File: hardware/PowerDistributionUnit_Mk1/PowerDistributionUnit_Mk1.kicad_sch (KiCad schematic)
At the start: 29 parts, among them J1 XT-30, J2 Molex_NanoFit_2x8, J3 Molex_NanoFit_1x4, J4 Molex_NanoFit_1x2, J5 Molex_NanoFit_1x2, J8 Molex_NanoFit_1x2, J9 Molex_NanoFit_1x2

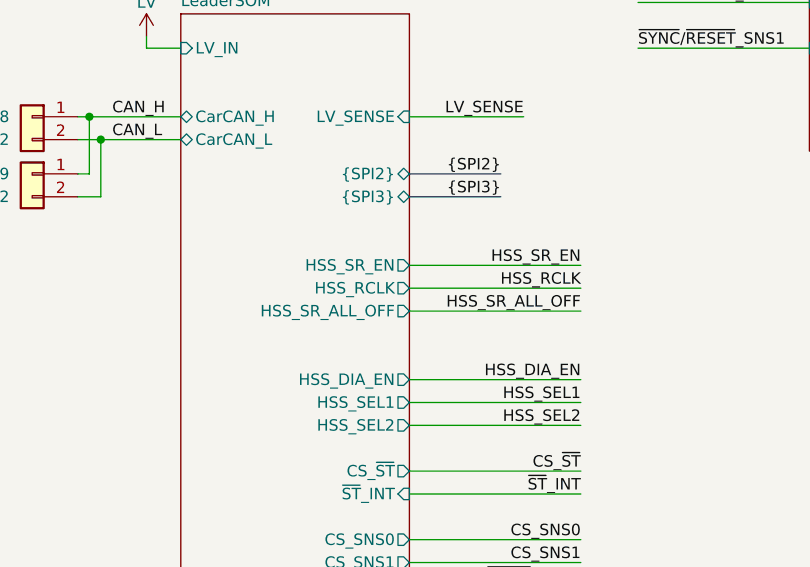
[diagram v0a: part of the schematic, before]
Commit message: routed a couple of logic analyzer connectors, fixed HSS SR out clk label, adjusted logic analyzer pinout
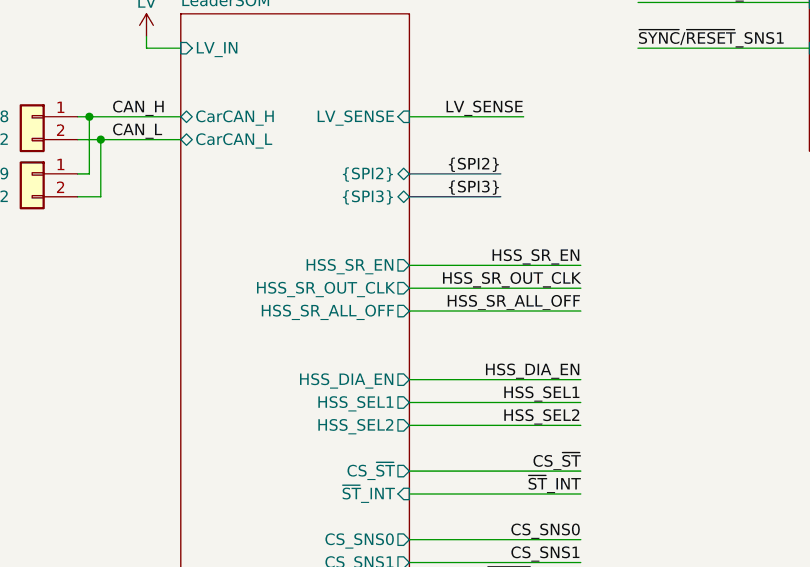
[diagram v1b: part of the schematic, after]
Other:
- sheet LeaderSOM ports: added HSS_SR_OUT_CLK; removed HSS_RCLK
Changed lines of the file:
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@@
 		)
 	)
-	(label "HSS_RCLK"
+	(label "HSS_SR_OUT_CLK"
 		(at 104.14 115.57 180)
 		(effects
@@
 			)
 		)
-		(pin "HSS_RCLK" output
+		(pin "HSS_SR_OUT_CLK" output
 			(at 85.09 115.57 0)
 			(effects

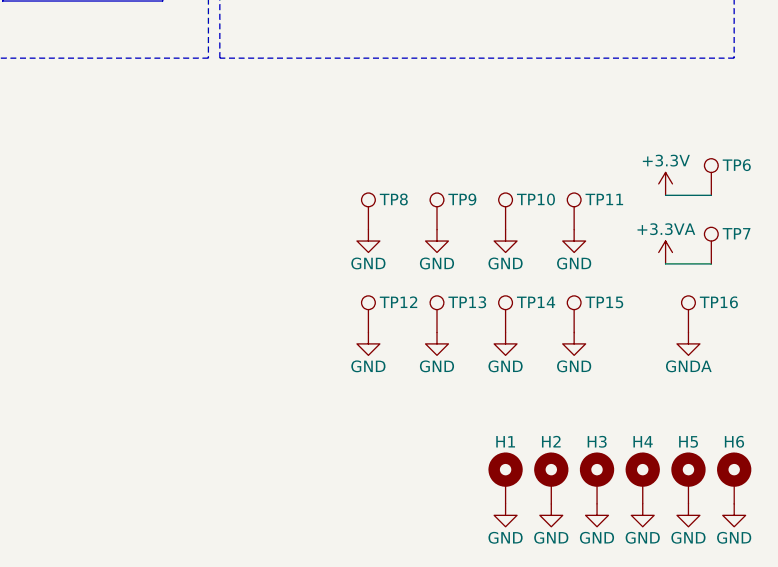
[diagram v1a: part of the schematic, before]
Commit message: gnd test points placement and added some
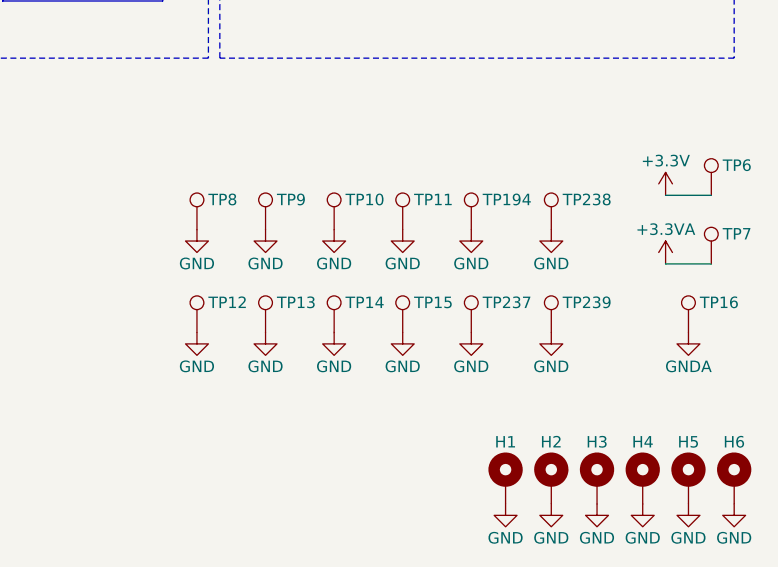
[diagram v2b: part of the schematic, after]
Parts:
- added TP194, TP237, TP238, TP239: TestPoint, Connector_PinHeader_2.54mm:PinHeader_1x01_P2.54mm_Vertical, symbol Connector:TestPoint
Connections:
- net GND: now also TP194.1, TP237.1, TP238.1, TP239.1
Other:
- moved on the sheet: TP10, TP11, TP12, TP13, TP14, TP15, TP8, TP9

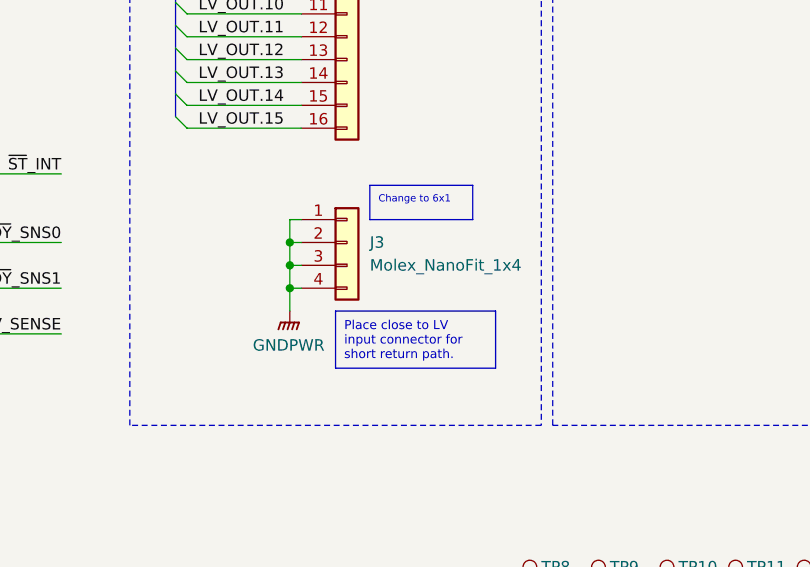
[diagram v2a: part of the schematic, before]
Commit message: change gnd return to 6 pin nanofit
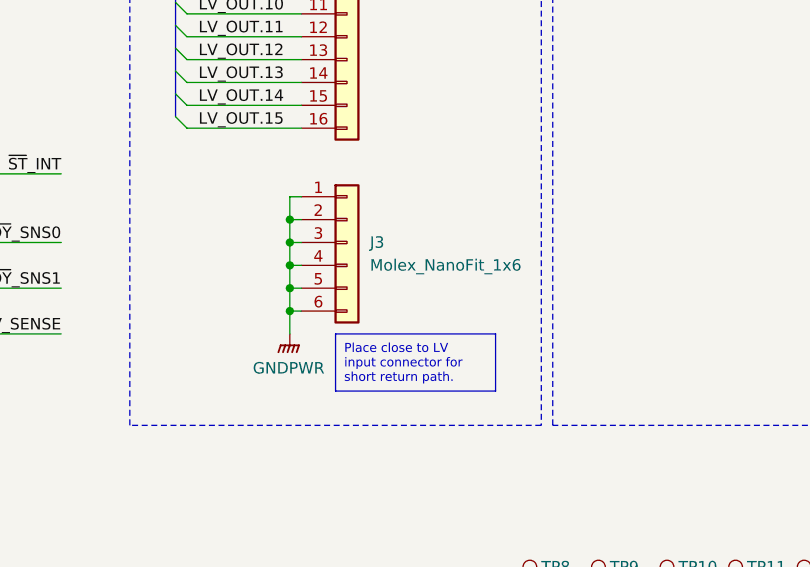
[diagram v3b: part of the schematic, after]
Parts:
- removed J3: Molex_NanoFit_1x4, PowerDistributionUnitLib:CONN_SD-105309-100_04_MOL, symbol PowerDistributionUnitLib:Molex_NanoFit_1x4
- added J3: Molex_NanoFit_1x6, PowerDistributionUnitLib:CONN_SD-105309-100_06_MOL, symbol PowerDistributionUnitLib:Molex_NanoFit_1x6
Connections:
- net GNDPWR: now also J3.1 (Pin_1), J3.2 (Pin_2), J3.3 (Pin_3), J3.4 (Pin_4), J3.5 (Pin_5), J3.6 (Pin_6)
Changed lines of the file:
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@@
 	(text_box "Place close to LV input connector for short return path."
 		(exclude_from_sim no)
-		(at 195.58 93.98 0)
+		(at 195.58 96.52 0)
 		(size 17.78 6.35)
 		(margins 0.9525 0.9525 0.9525 0.9525)
@@
 		)
 	)
-	(text_box "Change to 6x1"
-		(exclude_from_sim no)
-		(at 199.39 80.01 0)
-		(size 11.43 3.81)
-		(margins 0.9525 0.9525 0.9525 0.9525)
-		(stroke
-			(width 0)
-			(type solid)
-			(color 255 0 0 1)
-		)
-		(fill
-			(type none)
-		)
-		(effects
-			(font
-				(size 0.8 0.8)
-				(color 255 0 0 1)
-			)
-			(justify left top)
-		)
-	)
 	(junction
 		(at 176.53 29.21)
@@
 	)
 	(junction
+		(at 190.5 83.82)
+		(diameter 0)
+		(color 0 0 0 0)
+	)
+	(junction
+		(at 190.5 86.36)
+		(diameter 0)
+		(color 0 0 0 0)
+	)
+	(junction
 		(at 77.47 29.21)
 		(diameter 0)
@@
 	)
 	(junction
-		(at 190.5 91.44)
+		(at 190.5 93.98)
 		(diameter 0)
 		(color 0 0 0 0)
 	)
 	(junction
-		(at 190.5 86.36)
+		(at 190.5 88.9)
 		(diameter 0)
 		(color 0 0 0 0)
 	)
 	(junction
-		(at 190.5 88.9)
+		(at 190.5 91.44)
 		(diameter 0)
 		(color 0 0 0 0)
@@
 	(wire
 		(pts
-			(xy 190.5 88.9) (xy 190.5 91.44)
+			(xy 190.5 91.44) (xy 190.5 93.98)
 		)
 		(stroke
@@
 	(wire
 		(pts
-			(xy 190.5 83.82) (xy 191.77 83.82)
+			(xy 190.5 86.36) (xy 191.77 86.36)
 		)
 		(stroke
@@
 	(wire
 		(pts
+			(xy 190.5 83.82) (xy 191.77 83.82)
+		)
+		(stroke
+			(width 0)
+			(type default)
+		)
+	)
+	(wire
+		(pts
 			(xy 179.07 45.72) (xy 191.77 45.72)
 		)
@@
 	(wire
 		(pts
-			(xy 190.5 86.36) (xy 190.5 88.9)
+			(xy 190.5 88.9) (xy 190.5 91.44)
 		)
 		(stroke
@@
 	(wire
 		(pts
-			(xy 190.5 86.36) (xy 191.77 86.36)
+			(xy 190.5 81.28) (xy 190.5 83.82)
+		)
+		(stroke
+			(width 0)
+			(type default)
+		)
+	)
+	(wire
+		(pts
+			(xy 190.5 88.9) (xy 191.77 88.9)
 		)
 		(stroke
@@
 	(wire
 		(pts
-			(xy 190.5 91.44) (xy 191.77 91.44)
+			(xy 190.5 93.98) (xy 191.77 93.98)
 		)
 		(stroke
@@
 	(wire
 		(pts
+			(xy 190.5 81.28) (xy 191.77 81.28)
+		)
+		(stroke
+			(width 0)
+			(type default)
+		)
+	)
+	(wire
+		(pts
 			(xy 25.4 31.75) (xy 27.94 31.75)
 		)
@@
 	(wire
 		(pts
-			(xy 190.5 83.82) (xy 190.5 86.36)
+			(xy 190.5 86.36) (xy 190.5 88.9)
 		)
 		(stroke
@@
 	(wire
 		(pts
-			(xy 190.5 91.44) (xy 190.5 93.98)
+			(xy 190.5 93.98) (xy 190.5 96.52)
 		)
 		(stroke
@@
 		)
 	)
+	(wire
+		(pts
+			(xy 190.5 83.82) (xy 190.5 86.36)
+		)
+		(stroke
+			(width 0)
+			(type default)
+		)
+	)
 	(bus
 		(pts
@@
 	(wire
 		(pts
-			(xy 190.5 88.9) (xy 191.77 88.9)
+			(xy 190.5 91.44) (xy 191.77 91.44)
 		)
 		(stroke
@@
 	(symbol
 		(lib_id "power:GNDPWR")
-		(at 190.5 93.98 0)
+		(at 190.5 96.52 0)
 		(unit 1)
 		(exclude_from_sim no)
@@
 		(fields_autoplaced yes)
 		(property "Reference" "#PWR0459"
-			(at 190.5 99.06 0)
+			(at 190.5 101.6 0)
 			(effects
 				(font
@@
 		)
 		(property "Value" "GNDPWR"
-			(at 190.373 97.79 0)
+			(at 190.373 100.33 0)
 			(effects
 				(font
@@
 		)
 		(property "Footprint" ""
-			(at 190.5 95.25 0)
+			(at 190.5 97.79 0)
 			(effects
 				(font
@@
 		)
 		(property "Datasheet" ""
-			(at 190.5 95.25 0)
+			(at 190.5 97.79 0)
 			(effects
 				(font
@@
 		)
 		(property "Description" "Power symbol creates a global label with name \"GNDPWR\" , global ground"
-			(at 190.5 93.98 0)
+			(at 190.5 96.52 0)
 			(effects
 				(font
@@
 	)
 	(symbol
+		(lib_id "PowerDistributionUnitLib:Molex_NanoFit_1x6")
+		(at 196.85 86.36 0)
+		(unit 1)
+		(exclude_from_sim no)
+		(in_bom yes)
+		(on_board yes)
+		(dnp no)
+		(fields_autoplaced yes)
+		(property "Reference" "J3"
+			(at 199.39 86.3599 0)
+			(effects
+				(font
+					(size 1.27 1.27)
+				)
+				(justify left)
+			)
+		)
+		(property "Value" "Molex_NanoFit_1x6"
+			(at 199.39 88.8999 0)
+			(effects
+				(font
+					(size 1.27 1.27)
+				)
+				(justify left)
+			)
+		)
+		(property "Footprint" "PowerDistributionUnitLib:CONN_SD-105309-100_06_MOL"
+			(at 196.85 86.36 0)
+			(effects
+				(font
+					(size 1.27 1.27)
+				)
+				(hide yes)
+			)
+		)
+		(property "Datasheet" "kicad-embed://1053091206.pdf"
+			(at 196.85 86.36 0)
+			(effects
+				(font
+					(size 1.27 1.27)
+				)
+				(hide yes)
+			)
+		)
+		(property "Description" "Generic connector, single row, 01x06, script generated (kicad-library-utils/schlib/autogen/connector/)"
+			(at 196.85 86.36 0)
+			(effects
+				(font
+					(size 1.27 1.27)
+				)
+				(hide yes)
+			)
+		)
+		(property "P/N" "1053091206"
+			(at 196.85 86.36 0)
+			(effects
+				(font
+					(size 1.27 1.27)
+				)
+				(hide yes)
+			)
+		)
+		(property "Mouser P/N" "538-105309-1206"
+			(at 196.85 86.36 0)
+			(effects
+				(font
+					(size 1.27 1.27)
+				)
+				(hide yes)
+			)
+		)
+		(property "Digikey P/N" "WM14968-ND"
+			(at 196.85 86.36 0)
+			(effects
+				(font
+					(size 1.27 1.27)
+				)
+				(hide yes)
+			)
+		)
+		(pin "1"
+		)
+		(pin "2"
+		)
+		(pin "3"
+		)
+		(pin "4"
+		)
+		(pin "5"
+		)
+		(pin "6"
+		)
+		(instances
+			(project ""
+				(path "/6abaf095-8ba7-4306-8425-59a9eb37aa2b"
+					(reference "J3")
+					(unit 1)
+				)
+			)
+		)
+	)
+	(symbol
 		(lib_id "Mechanical:MountingHole_Pad")
 		(at 271.78 153.67 0)
@@
 					(unit 1)
 				)
-			)
-		)
-	)
-	(symbol
-		(lib_id "PowerDistributionUnitLib:Molex_NanoFit_1x4")
-		(at 196.85 86.36 0)
-		(unit 1)
-		(exclude_from_sim no)
-		(in_bom yes)
-		(on_board yes)
-		(dnp no)
-		(fields_autoplaced yes)
-		(property "Reference" "J3"
-			(at 199.39 86.3599 0)
-			(effects
-				(font
-					(size 1.27 1.27)
-				)
-				(justify left)
-			)
-		)
-		(property "Value" "Molex_NanoFit_1x4"
-			(at 199.39 88.8999 0)
-			(effects
-				(font
-					(size 1.27 1.27)
-				)
-				(justify left)
-			)
-		)
-		(property "Footprint" "PowerDistributionUnitLib:CONN_SD-105309-100_04_MOL"
-			(at 196.85 86.36 0)
-			(effects
-				(font
-					(size 1.27 1.27)
-				)
-				(hide yes)
-			)
-		)
-		(property "Datasheet" "kicad-embed://1053121116.stp"
-			(at 196.85 86.36 0)
-			(effects
-				(font
-					(size 1.27 1.27)
-				)
-				(hide yes)
-			)
-		)
-		(property "Description" "Generic connector, single row, 01x04, script generated (kicad-library-utils/schlib/autogen/connector/)"
-			(at 196.85 86.36 0)
-			(effects
-				(font
-					(size 1.27 1.27)
-				)
-				(hide yes)
-			)
-		)
-		(property "P/N" "105309-1104"
-			(at 196.85 86.36 0)
-			(effects
-				(font
-					(size 1.27 1.27)
-				)
-				(hide yes)
-			)
-		)
-		(property "Mouser P/N" "538-105309-1104"
-			(at 196.85 86.36 0)
-			(effects
-				(font
-					(size 1.27 1.27)
-				)
-				(hide yes)
-			)
-		)
-		(property "Digikey P/N" ""
-			(at 196.85 86.36 0)
-			(effects
-				(font
-					(size 1.27 1.27)
-				)
-				(hide yes)
-			)
-		)
-		(pin "3"
-		)
-		(pin "1"
-		)
-		(pin "2"
-		)
-		(pin "4"
-		)
-		(instances
-			(project ""
-				(path "/6abaf095-8ba7-4306-8425-59a9eb37aa2b"
-					(reference "J3")
-					(unit 1)
-				)
